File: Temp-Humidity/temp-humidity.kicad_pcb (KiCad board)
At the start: 2 copper layers, 54 x 29 mm, 28 parts, among them IC1 ATMEGA328P-A, P1 BATTERY, P2 CONN_02X03, P3 SERIAL/DEBUG, P4 ANTENNA, SW1 SW_PUSH_SMALL_H, U1 AT25DF512, U2 HDC1080, U3 ATSHA204A, U4 NRF24L01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

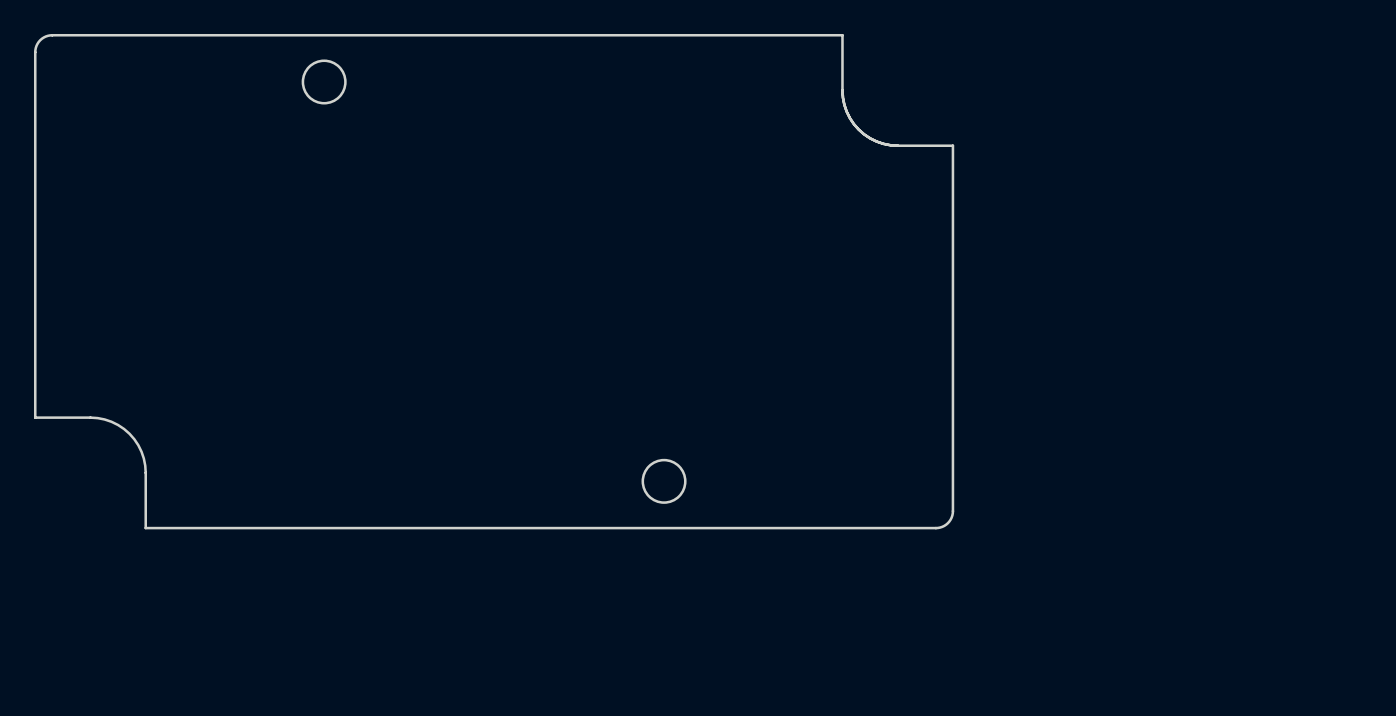
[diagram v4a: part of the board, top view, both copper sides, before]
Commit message: pcb edge cut with this box : http://www.farnell.com/datasheets/682682.pdf
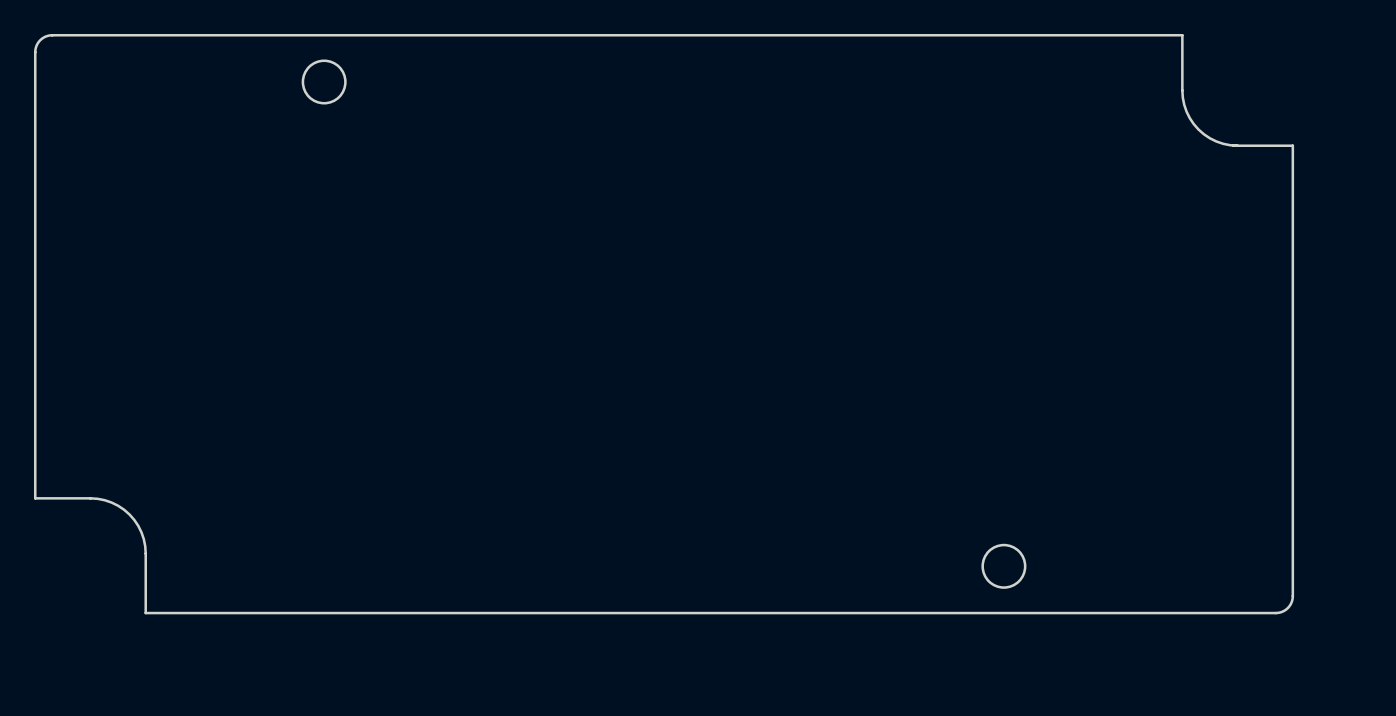
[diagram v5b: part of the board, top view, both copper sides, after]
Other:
- board size 54 x 29 mm -> 74 x 34 mm
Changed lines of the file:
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@@
     (links 85)
     (no_connects 63)
-    (area 69.665432 66.66324 103.723061 122.871701)
+    (area 182.398599 29.135399 211.548601 83.285401)
     (thickness 1.6)
-    (drawings 15)
+    (drawings 14)
     (tracks 0)
     (zones 0)
@@
     )
   )
-  (gr_circle (center 37 26.25) (end 38.25 26.25) (layer Edge.Cuts) (width 0.15))
-  (gr_circle (center 17 2.75) (end 18.25 2.75) (layer Edge.Cuts) (width 0.15))
-  (gr_line (start 6.5 25.75) (end 6.5 29) (angle 90) (layer Edge.Cuts) (width 0.15))
-  (gr_arc (start 3.25 25.75) (end 6.5 25.75) (angle -90) (layer Edge.Cuts) (width 0.15))
-  (gr_line (start 0 22.5) (end 3.25 22.5) (angle 90) (layer Edge.Cuts) (width 0.15))
-  (gr_arc (start 50.75 3.25) (end 50.75 6.5) (angle 90) (layer Edge.Cuts) (width 0.15))
-  (gr_arc (start 50.75 3.25) (end 50.75 6.5) (angle 90) (layer Edge.Cuts) (width 0.15))
-  (gr_line (start 50.75 6.5) (end 54 6.5) (angle 90) (layer Edge.Cuts) (width 0.15))
-  (gr_line (start 47.5 0) (end 47.5 3.25) (angle 90) (layer Edge.Cuts) (width 0.15))
+  (gr_line (start 0 27.25) (end 0 1) (angle 90) (layer Edge.Cuts) (width 0.15))
+  (gr_line (start 73 34) (end 6.5 34) (angle 90) (layer Edge.Cuts) (width 0.15))
+  (gr_line (start 74 6.5) (end 74 33) (angle 90) (layer Edge.Cuts) (width 0.15))
+  (gr_line (start 1 0) (end 67.5 0) (angle 90) (layer Edge.Cuts) (width 0.15))
+  (gr_circle (center 17 2.75) (end 17 4) (layer Edge.Cuts) (width 0.15))
+  (gr_circle (center 57 31.25) (end 57 32.5) (layer Edge.Cuts) (width 0.15))
+  (gr_line (start 67.5 3.25) (end 67.5 0) (angle 90) (layer Edge.Cuts) (width 0.15))
+  (gr_arc (start 70.75 3.25) (end 67.5 3.25) (angle -90) (layer Edge.Cuts) (width 0.15))
+  (gr_line (start 74 6.5) (end 70.5 6.5) (angle 90) (layer Edge.Cuts) (width 0.15))
+  (gr_arc (start 3.25 30.5) (end 3.25 27.25) (angle 90) (layer Edge.Cuts) (width 0.15))
+  (gr_line (start 3.25 27.25) (end 0 27.25) (angle 90) (layer Edge.Cuts) (width 0.15))
+  (gr_line (start 6.5 34) (end 6.5 30.5) (angle 90) (layer Edge.Cuts) (width 0.15))
+  (gr_arc (start 73 33) (end 74 33) (angle 90) (layer Edge.Cuts) (width 0.15))
   (gr_arc (start 1 1) (end 0 1) (angle 90) (layer Edge.Cuts) (width 0.15))
-  (gr_arc (start 53 28) (end 54 28) (angle 90) (layer Edge.Cuts) (width 0.15))
-  (gr_line (start 0 1) (end 0 22.5) (angle 90) (layer Edge.Cuts) (width 0.15))
-  (gr_line (start 6.5 29) (end 53 29) (angle 90) (layer Edge.Cuts) (width 0.15))
-  (gr_line (start 54 6.5) (end 54 28) (angle 90) (layer Edge.Cuts) (width 0.15))
-  (gr_line (start 1 0) (end 47.5 0) (angle 90) (layer Edge.Cuts) (width 0.15))
   (zone (net 0) (net_name "") (layer F.Cu) (hatch edge 0.508)
     (connect_pads (clearance 0.508))

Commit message: More work on hum/temp
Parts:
- added REF**: MountingHole_2.5mm, Mounting_Holes:MountingHole_2.5mm, F.Cu at (142.3, 62.7)
- added REF**: MountingHole_2.5mm, Mounting_Holes:MountingHole_2.5mm, F.Cu at (113.8, 102.7)
- moved U3 82.2 mm to (122.2, 50.3), turned to 90 degrees
- moved IC1 81.6 mm to (127.3, 86.4)
- moved C4 80.8 mm to (120.1, 71.9)
- moved C1 79.1 mm to (117.7, 66.2), turned to 0 degrees
- moved P4 78.9 mm to (113.6, 109.8)
- moved U4 78.1 mm to (128.0, 110.4)
- moved D1 78.0 mm to (128.0, 67.6), turned to 0 degrees
- moved C3 77.7 mm to (117.7, 60.4), turned to 0 degrees
- moved R3 77.4 mm to (115.8, 71.9)
- moved U5 77.3 mm to (119.8, 95.5)
- moved JP1 76.7 mm to (113.0, 90.0)
- moved P3 76.7 mm to (113.0, 71.2)
- moved P1 73.8 mm to (140.4, 52.7)
- moved C5 73.8 mm to (123.7, 78.2)
- moved Y1 73.1 mm to (126.7, 74.9)
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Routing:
- net +3V3: track 0.00 -> 173.3 mm, vias 0 -> 12
- net GND: track 0.00 -> 123.1 mm, vias 0 -> 10
- net /SCK: track 0.00 -> 63.8 mm, vias 0 -> 8
- net /MOSI: track 0.00 -> 61.3 mm, vias 0 -> 7
- net /SDA: track 0.00 -> 51.5 mm, vias 0 -> 6
- net /BTN1: track 0.00 -> 46.9 mm
- net /IRQ: track 0.00 -> 38.7 mm, vias 0 -> 4
- net Net-(C6-Pad2): track 0.00 -> 30.2 mm, vias 0 -> 4
- net /MISO: track 0.00 -> 27.1 mm, vias 0 -> 2
- net /CSN: track 0.00 -> 26.8 mm, vias 0 -> 2
- net Net-(C4-Pad1): track 0.00 -> 26.6 mm, vias 0 -> 2
- net Net-(IC1-Pad2): track 0.00 -> 25.1 mm, vias 0 -> 2
- net /DTR: track 0.00 -> 24.4 mm, vias 0 -> 2
- net /FLASH_CS: track 0.00 -> 23.6 mm, vias 0 -> 2
- net /TX: track 0.00 -> 20.6 mm, vias 0 -> 2
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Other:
- board size 74 x 34 mm -> 34 x 74 mm

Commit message: More work on hum/temp
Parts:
- removed REF** (x2): MountingHole_2.5mm, Mounting_Holes:MountingHole_2.5mm
- P1: moved to F.Cu
- Y1: footprint Crystals:Crystal_SMD_5032_2Pads -> mysensors_obscurities:XTAL_3.2x1.5mm
- moved C2 39.4 mm to (135.1, 87.4), turned to 90 degrees
- moved C3 35.7 mm to (125.2, 95.2)
- moved U2 32.3 mm to (119.1, 75.4), turned to 0 degrees
- moved R5 31.0 mm to (128.3, 79.0), turned to 0 degrees
- moved U3 30.1 mm to (137.9, 76.0)
- moved C1 29.1 mm to (119.6, 95.2), turned to 180 degrees
- moved R6 28.9 mm to (138.2, 80.0), turned to 180 degrees
- moved R4 19.4 mm to (131.0, 95.2), turned to 0 degrees
- moved C6 18.7 mm to (117.3, 91.4)
- moved R7 17.6 mm to (139.2, 93.2)
- moved P2 17.6 mm to (137.9, 85.1)
- moved Y1 16.0 mm to (121.2, 89.9), turned to 270 degrees
- moved U1 15.0 mm to (128.2, 74.2), turned to 180 degrees
- moved R1 13.6 mm to (136.4, 64.3), turned to 0 degrees
- moved P1 13.2 mm to (128.0, 48.0), turned to 0 degrees
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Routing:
- net Net-(C6-Pad2): track 30.2 -> 6.77 mm, vias 4 -> 0
- net /SCK: track 63.8 -> 40.5 mm, vias 8 -> 5
- net /MOSI: track 61.3 -> 38.3 mm, vias 7 -> 5
- net +3V3: track 173.3 -> 153.4 mm, vias 12 -> 11
- net GND: track 123.1 -> 142.0 mm, vias 10 -> 9
- net /FLASH_CS: track 23.6 -> 10.0 mm
- net /BTN1: track 46.9 -> 33.7 mm
- net Net-(C5-Pad2): track 17.8 -> 5.80 mm
- net /SDA: track 51.5 -> 41.5 mm, vias 6 -> 4
- net /TX: track 20.6 -> 16.7 mm, vias 2 -> 1
- net /DTR: track 24.4 -> 21.3 mm, vias 2 -> 1
- net /IRQ: track 38.7 -> 41.8 mm
- net /CSN: track 26.8 -> 23.8 mm
- net VDD: track 13.1 -> 10.0 mm
- net Net-(D1-Pad1): track 8.65 -> 5.78 mm, vias 2 -> 0
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- removed copper zone on B.Cu, net GND

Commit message: work++
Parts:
- moved C1 22.6 mm to (142.0, 98.8), turned to 270 degrees
- moved U2 18.3 mm to (136.7, 70.1), turned to 270 degrees
- moved R5 15.5 mm to (141.5, 70.9), turned to 90 degrees
- moved C4 13.5 mm to (135.1, 82.8)
- moved IC1 12.6 mm to (128.8, 73.9)
- moved U1 12.2 mm to (127.0, 86.4), turned to 270 degrees
- moved R4 10.2 mm to (132.1, 85.1), turned to 90 degrees
- moved D1 9.80 mm to (119.9, 62.0), turned to 90 degrees
- moved C3 9.34 mm to (116.6, 98.8), turned to 90 degrees
- moved P1 4.93 mm to (129.0, 52.8), turned to 180 degrees
- moved R3 4.79 mm to (117.9, 80.3)
- moved R2 3.84 mm to (119.9, 67.6), turned to 270 degrees
- moved R6 1.93 mm to (140.0, 80.8)
- moved P4 1.55 mm to (114.3, 111.0)
- moved R1 1.48 mm to (135.6, 63.0), turned to 90 degrees
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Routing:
- net GND: track 142.0 -> 27.6 mm, vias 9 -> 2
- net +3V3: track 153.4 -> 119.4 mm, vias 11 -> 4
- net /MISO: track 26.2 -> 50.2 mm, vias 2 -> 7
- net /SCK: track 40.5 -> 61.7 mm, vias 5 -> 4
- net /MOSI: track 38.3 -> 59.5 mm
- net /SDA: track 41.5 -> 22.6 mm
- net Net-(IC1-Pad2): track 24.9 -> 5.99 mm
- net /CSN: track 23.8 -> 41.4 mm, vias 2 -> 6
- net /CE: track 13.0 -> 30.3 mm
- net /IRQ: track 41.8 -> 55.1 mm, vias 4 -> 6
- net Net-(C4-Pad1): track 25.5 -> 13.0 mm
- net Net-(C6-Pad2): track 6.77 -> 18.8 mm
- net /SCL: track 3.79 -> 15.4 mm, vias 0 -> 2
- net Net-(C5-Pad2): track 5.80 -> 17.2 mm
- net /BTN1: track 33.7 -> 23.4 mm, vias 0 -> 2
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- added copper zone on B.Cu, net +3V3
- added copper zone on F.Cu, net GND
- removed copper zone on F.Cu, net +3V3
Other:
- net class Default: trace_width 0.25 -> 0.2; via_dia 0.6 -> 0.4; via_drill 0.4 -> 0.3
